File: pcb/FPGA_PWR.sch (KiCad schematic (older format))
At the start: 43 parts, among them U4 iCE40-HX8K-CT256, U8 AZ1117EH-ADJ

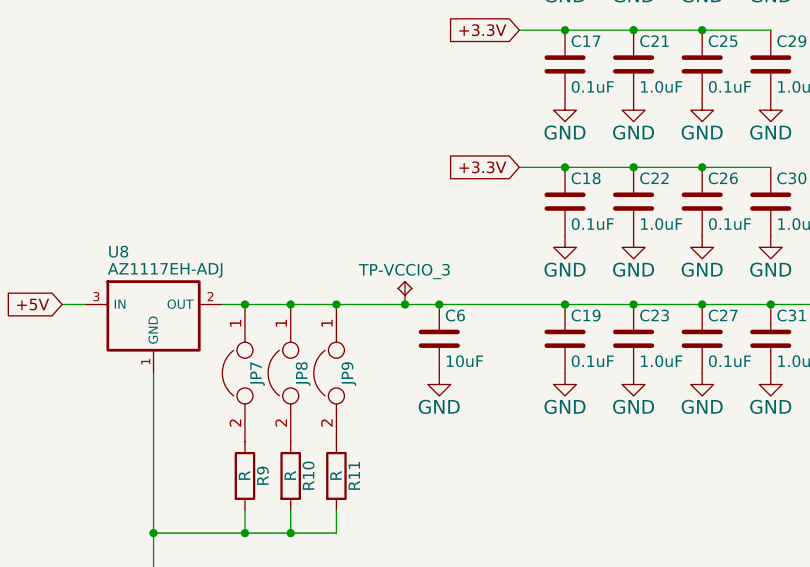
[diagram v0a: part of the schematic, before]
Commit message: Silkscreen done, test points added.
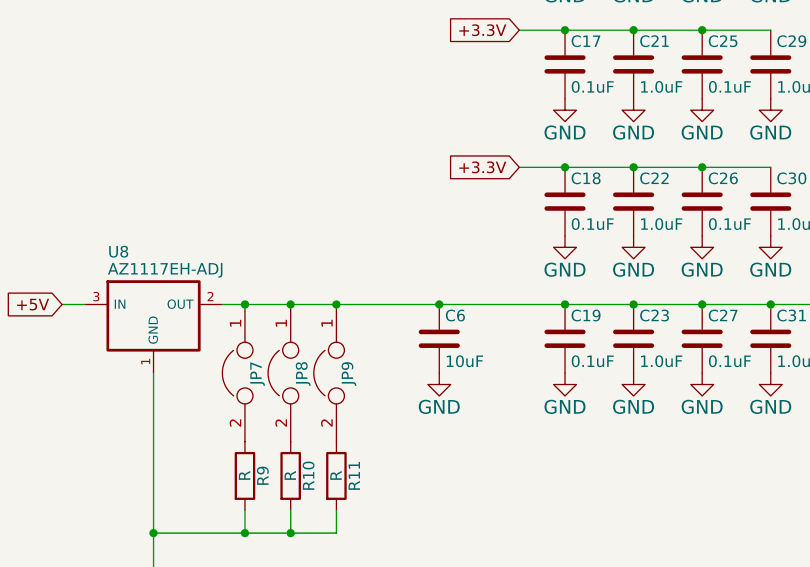
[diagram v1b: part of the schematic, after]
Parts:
- removed TP-VCCIO_3: TPTP-COMPACT, Measurement_Points:Measurement_Point_Round-TH_Small, symbol TPTP-COMPACT
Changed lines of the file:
@@
 1E 25 49 2A DA F6 C4 5C B7 0C C3 B9 A4 0A 98 09 FC 0D B0 92 CD 57 CD 1F 06 4E 04 26 A7 75 27 49
 52 39 26 13 73 DE C3 6C BE 70 B5 12 F8 16 86 73 8D C3 FF 03 63 F8 EE 2E BE 9A 04 B1 00 00 00 00
-49 45 4E 44 AE 42 60 82 73
+49 45 4E 44 AE 42 60 82 8C
 EndData
 $EndBitmap
@@
 $EndComp
 $Comp
-L TPTP-COMPACT TP-VCCIO_?
-U 1 1 55FBE808
-P 3500 5500
-AR Path="/55FBE808" Ref="TP-VCCIO_?"  Part="1"
-AR Path="/55DF5F27/55E883EA/55F049E0/55FBE808" Ref="TP-VCCIO_3"  Part="1"
-F 0 "TP-VCCIO_3" H 3500 5650 50  0000 C CNN
-F 1 "TPTP-COMPACT" H 3500 5500 50  0001 L BNN
-F 2 "Measurement_Points:Measurement_Point_Round-TH_Small" H 3500 5650 50  0001 C CNN
-F 3 "" H 3500 5500 60  0000 C CNN
-	1    3500 5500
-	1    0    0    -1
-$EndComp
-Connection ~ 3500 5500
-$Comp
 L C C6

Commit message: Generated the gerbers and submitted them. * Added some 3D models.
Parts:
- JP7, JP8, JP9: footprint open-project:S_JUMPER_2 -> XESS:S_JUMPER_2
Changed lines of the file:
@@
 1E 25 49 2A DA F6 C4 5C B7 0C C3 B9 A4 0A 98 09 FC 0D B0 92 CD 57 CD 1F 06 4E 04 26 A7 75 27 49
 52 39 26 13 73 DE C3 6C BE 70 B5 12 F8 16 86 73 8D C3 FF 03 63 F8 EE 2E BE 9A 04 B1 00 00 00 00
-49 45 4E 44 AE 42 60 82 8C
+49 45 4E 44 AE 42 60 82 40
 EndData
 $EndBitmap
@@
 F 0 "JP7" H 2800 5750 50  0000 C CNN
 F 1 "JUMPER" H 2800 5720 50  0001 C CNN
-F 2 "open-project:S_JUMPER_2" H 2800 5800 60  0001 C CNN
+F 2 "XESS:S_JUMPER_2" H 2800 5800 60  0001 C CNN
 F 3 "" H 2800 5800 60  0000 C CNN
 	1    2800 5800
@@
 F 0 "JP8" H 3000 5750 50  0000 C CNN
 F 1 "JUMPER" H 3000 5720 50  0001 C CNN
-F 2 "open-project:S_JUMPER_2" H 3000 5800 60  0001 C CNN
+F 2 "XESS:S_JUMPER_2" H 3000 5800 60  0001 C CNN
 F 3 "" H 3000 5800 60  0000 C CNN
 	1    3000 5800
@@
 F 0 "JP9" H 3200 5750 50  0000 C CNN
 F 1 "JUMPER" H 3200 5720 50  0001 C CNN
-F 2 "open-project:S_JUMPER_2" H 3200 5800 60  0001 C CNN
+F 2 "XESS:S_JUMPER_2" H 3200 5800 60  0001 C CNN
 F 3 "" H 3200 5800 60  0000 C CNN
 	1    3200 5800

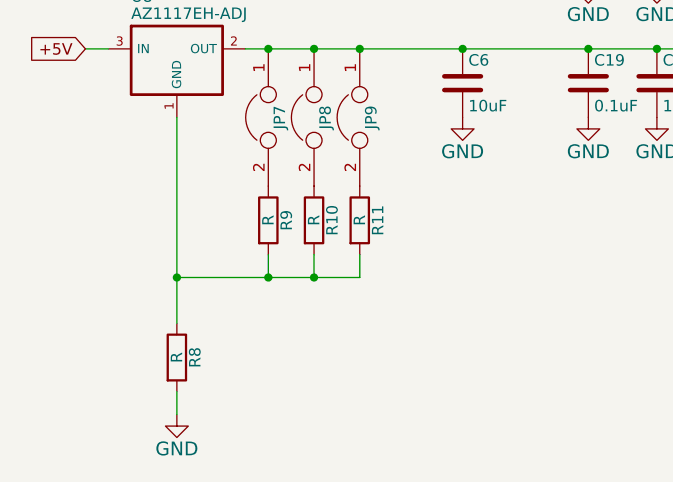
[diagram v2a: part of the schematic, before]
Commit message: Added manufacturer part numbers to the schematic.
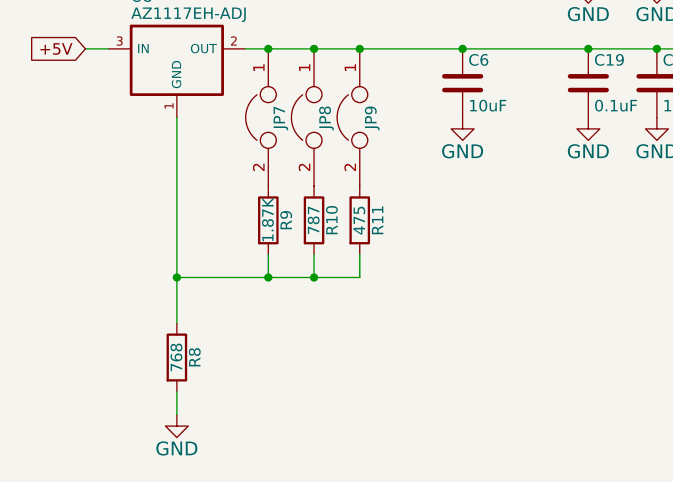
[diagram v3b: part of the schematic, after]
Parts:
- C16: manf# 08055C104KAT2A -> GRM188R71C104KA01D
- C17, C18, C19, C21, C22, C23, C24, C25, C26, C27, C28, C29, C30, C31, C32, C33, C34, C35, C38, C39, C40, C41, C42, C44, C45, C46: manf# 08055C104KAT2A -> (none)
- C20: manf# 08055C104KAT2A -> GRM188R71C105KE15D
- C43: manf# 08055C104KAT2A -> GRM188R71H103KA01D
- C6: manf# LMK212BJ106KD-T -> (none)
- D1: manf# (none) -> 1N4448WX-TP
- R10: value R -> 787; manf# (none) -> RC0603FR-07787RL
- R11: value R -> 475; manf# (none) -> RC0603FR-07475RL
- R8: value R -> 768; manf# (none) -> RC0603FR-07768RL
- R9: value R -> 1.87K; manf# (none) -> RC0603FR-071K87L
- U4: manf# (none) -> ICE40HX8K-CT256
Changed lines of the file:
@@
 F 2 "XESS:Lattice_caBGA_256" H 6700 2100 60  0001 C CNN
 F 3 "" H 6700 2100 60  0000 C CNN
+F 4 "ICE40HX8K-CT256" H 6700 2100 60  0001 C CNN "manf#"
 	1    6700 2100
 	1    0    0    -1
@@
 F 2 "Capacitors_SMD:C_0603" H 4238 3700 30  0001 C CNN
 F 3 "" H 4200 3850 60  0000 C CNN
-F 4 "08055C104KAT2A" H 4200 3850 60  0001 C CNN "manf#"
+F 4 "GRM188R71C104KA01D" H 4200 3850 60  0001 C CNN "manf#"
 	1    4200 3850
 	1    0    0    -1
@@
 F 2 "Capacitors_SMD:C_0603" H 4538 3700 30  0001 C CNN
 F 3 "" H 4500 3850 60  0000 C CNN
-F 4 "08055C104KAT2A" H 4500 3850 60  0001 C CNN "manf#"
+F 4 "GRM188R71C105KE15D" H 4500 3850 60  0001 C CNN "manf#"
 	1    4500 3850
 	1    0    0    -1
@@
 F 2 "Capacitors_SMD:C_0603" H 4838 3700 30  0001 C CNN
 F 3 "" H 4800 3850 60  0000 C CNN
-F 4 "08055C104KAT2A" H 4800 3850 60  0001 C CNN "manf#"
 	1    4800 3850
 	1    0    0    -1
@@
 F 2 "Capacitors_SMD:C_0603" H 5138 3700 30  0001 C CNN
 F 3 "" H 5100 3850 60  0000 C CNN
-F 4 "08055C104KAT2A" H 5100 3850 60  0001 C CNN "manf#"
 	1    5100 3850
 	1    0    0    -1
@@
 F 2 "Capacitors_SMD:C_0603" H 4238 4300 30  0001 C CNN
 F 3 "" H 4200 4450 60  0000 C CNN
-F 4 "08055C104KAT2A" H 4200 4450 60  0001 C CNN "manf#"
 	1    4200 4450
 	1    0    0    -1
@@
 F 2 "Capacitors_SMD:C_0603" H 4538 4300 30  0001 C CNN
 F 3 "" H 4500 4450 60  0000 C CNN
-F 4 "08055C104KAT2A" H 4500 4450 60  0001 C CNN "manf#"
 	1    4500 4450
 	1    0    0    -1
@@
 F 2 "Capacitors_SMD:C_0603" H 4838 4300 30  0001 C CNN
 F 3 "" H 4800 4450 60  0000 C CNN
-F 4 "08055C104KAT2A" H 4800 4450 60  0001 C CNN "manf#"
 	1    4800 4450
 	1    0    0    -1
@@
 F 2 "Capacitors_SMD:C_0603" H 5138 4300 30  0001 C CNN
 F 3 "" H 5100 4450 60  0000 C CNN
-F 4 "08055C104KAT2A" H 5100 4450 60  0001 C CNN "manf#"
 	1    5100 4450
 	1    0    0    -1
@@
 F 2 "Capacitors_SMD:C_0603" H 4238 4900 30  0001 C CNN
 F 3 "" H 4200 5050 60  0000 C CNN
-F 4 "08055C104KAT2A" H 4200 5050 60  0001 C CNN "manf#"
 	1    4200 5050
 	1    0    0    -1
@@
 F 2 "Capacitors_SMD:C_0603" H 4538 4900 30  0001 C CNN
 F 3 "" H 4500 5050 60  0000 C CNN
-F 4 "08055C104KAT2A" H 4500 5050 60  0001 C CNN "manf#"
 	1    4500 5050
 	1    0    0    -1
@@
 F 2 "Capacitors_SMD:C_0603" H 4838 4900 30  0001 C CNN
 F 3 "" H 4800 5050 60  0000 C CNN
-F 4 "08055C104KAT2A" H 4800 5050 60  0001 C CNN "manf#"
 	1    4800 5050
 	1    0    0    -1
@@
 F 2 "Capacitors_SMD:C_0603" H 5138 4900 30  0001 C CNN
 F 3 "" H 5100 5050 60  0000 C CNN
-F 4 "08055C104KAT2A" H 5100 5050 60  0001 C CNN "manf#"
 	1    5100 5050
 	1    0    0    -1
@@
 F 2 "Capacitors_SMD:C_0603" H 4238 5500 30  0001 C CNN
 F 3 "" H 4200 5650 60  0000 C CNN
-F 4 "08055C104KAT2A" H 4200 5650 60  0001 C CNN "manf#"
 	1    4200 5650
 	1    0    0    -1
@@
 F 2 "Capacitors_SMD:C_0603" H 4538 5500 30  0001 C CNN
 F 3 "" H 4500 5650 60  0000 C CNN
-F 4 "08055C104KAT2A" H 4500 5650 60  0001 C CNN "manf#"
 	1    4500 5650
 	1    0    0    -1
@@
 F 2 "Capacitors_SMD:C_0603" H 4838 5500 30  0001 C CNN
 F 3 "" H 4800 5650 60  0000 C CNN
-F 4 "08055C104KAT2A" H 4800 5650 60  0001 C CNN "manf#"
 	1    4800 5650
 	1    0    0    -1
@@
 F 2 "Capacitors_SMD:C_0603" H 5138 5500 30  0001 C CNN
 F 3 "" H 5100 5650 60  0000 C CNN
-F 4 "08055C104KAT2A" H 5100 5650 60  0001 C CNN "manf#"
 	1    5100 5650
 	1    0    0    -1
@@
 F 2 "Capacitors_SMD:C_0603" H 5588 1700 30  0001 C CNN
 F 3 "" H 5550 1850 60  0000 C CNN
-F 4 "08055C104KAT2A" H 5550 1850 60  0001 C CNN "manf#"
 	1    5550 1850
 	1    0    0    -1
@@
 F 2 "Capacitors_SMD:C_0805" H 5338 1700 30  0001 C CNN
 F 3 "" H 5300 1850 60  0000 C CNN
-F 4 "08055C104KAT2A" H 5300 1850 60  0001 C CNN "manf#"
 	1    5300 1850
 	1    0    0    -1
@@
 F 2 "Capacitors_SMD:C_0603" H 5588 2200 30  0001 C CNN
 F 3 "" H 5550 2350 60  0000 C CNN
-F 4 "08055C104KAT2A" H 5550 2350 60  0001 C CNN "manf#"
 	1    5550 2350
 	1    0    0    -1
@@
 F 2 "Capacitors_SMD:C_0805" H 5338 2200 30  0001 C CNN
 F 3 "" H 5300 2350 60  0000 C CNN
-F 4 "08055C104KAT2A" H 5300 2350 60  0001 C CNN "manf#"
 	1    5300 2350
 	1    0    0    -1
@@
 F 2 "Diodes_SMD:SOD-323" H 6550 2800 60  0001 C CNN
 F 3 "" H 6550 2800 60  0000 C CNN
+F 4 "1N4448WX-TP" H 6550 2800 60  0001 C CNN "manf#"
 	1    6550 2800
 	-1   0    0    1
@@
 F 2 "Capacitors_SMD:C_0603" H 6838 3700 30  0001 C CNN
 F 3 "" H 6800 3850 60  0000 C CNN
-F 4 "08055C104KAT2A" H 6800 3850 60  0001 C CNN "manf#"
 	1    6800 3850
 	1    0    0    -1
@@
 F 2 "Capacitors_SMD:C_0603" H 7138 3700 30  0001 C CNN
 F 3 "" H 7100 3850 60  0000 C CNN
-F 4 "08055C104KAT2A" H 7100 3850 60  0001 C CNN "manf#"
 	1    7100 3850
 	1    0    0    -1
@@
 F 2 "Capacitors_SMD:C_0603" H 7438 3700 30  0001 C CNN
 F 3 "" H 7400 3850 60  0000 C CNN
-F 4 "08055C104KAT2A" H 7400 3850 60  0001 C CNN "manf#"
 	1    7400 3850
 	1    0    0    -1
@@
 F 2 "Capacitors_SMD:C_0603" H 7738 3700 30  0001 C CNN
 F 3 "" H 7700 3850 60  0000 C CNN
-F 4 "08055C104KAT2A" H 7700 3850 60  0001 C CNN "manf#"
 	1    7700 3850
 	1    0    0    -1
@@
 F 2 "Capacitors_SMD:C_0603" H 8038 3700 30  0001 C CNN
 F 3 "" H 8000 3850 60  0000 C CNN
-F 4 "08055C104KAT2A" H 8000 3850 60  0001 C CNN "manf#"
 	1    8000 3850
 	1    0    0    -1
@@
 F 2 "Capacitors_SMD:C_0603" H 8338 3700 30  0001 C CNN
 F 3 "" H 8300 3850 60  0000 C CNN
-F 4 "08055C104KAT2A" H 8300 3850 60  0001 C CNN "manf#"
 	1    8300 3850
 	1    0    0    -1
@@
 F 2 "Capacitors_SMD:C_0603" H 6838 4300 30  0001 C CNN
 F 3 "" H 6800 4450 60  0000 C CNN
-F 4 "08055C104KAT2A" H 6800 4450 60  0001 C CNN "manf#"
 	1    6800 4450
 	1    0    0    -1
@@
 F 2 "Capacitors_SMD:C_0603" H 7138 4300 30  0001 C CNN
 F 3 "" H 7100 4450 60  0000 C CNN
-F 4 "08055C104KAT2A" H 7100 4450 60  0001 C CNN "manf#"
 	1    7100 4450
 	1    0    0    -1
@@
 F 2 "Capacitors_SMD:C_0603" H 7438 4300 30  0001 C CNN
 F 3 "" H 7400 4450 60  0000 C CNN
-F 4 "08055C104KAT2A" H 7400 4450 60  0001 C CNN "manf#"
+F 4 "GRM188R71H103KA01D" H 7400 4450 60  0001 C CNN "manf#"
 	1    7400 4450
 	1    0    0    -1
@@
 1E 25 49 2A DA F6 C4 5C B7 0C C3 B9 A4 0A 98 09 FC 0D B0 92 CD 57 CD 1F 06 4E 04 26 A7 75 27 49
 52 39 26 13 73 DE C3 6C BE 70 B5 12 F8 16 86 73 8D C3 FF 03 63 F8 EE 2E BE 9A 04 B1 00 00 00 00
-49 45 4E 44 AE 42 60 82 40
+49 45 4E 44 AE 42 60 82 13
 EndData
 $EndBitmap
@@
 F 2 "Capacitors_SMD:C_0805" H 3688 5500 30  0001 C CNN
 F 3 "" H 3650 5650 60  0000 C CNN
-F 4 "LMK212BJ106KD-T" H 3650 5650 60  0001 C CNN "manf#"
 	1    3650 5650
 	1    0    0    -1
@@
 P 2400 6850
 F 0 "R8" V 2480 6850 50  0000 C CNN
-F 1 "R" V 2400 6850 50  0000 C CNN
+F 1 "768" V 2400 6850 50  0000 C CNN
 F 2 "Resistors_SMD:R_0603" V 2330 6850 30  0001 C CNN
 F 3 "" H 2400 6850 30  0000 C CNN
+F 4 "RC0603FR-07768RL" V 2400 6850 60  0001 C CNN "manf#"
 	1    2400 6850
 	1    0    0    -1
@@
 P 2800 6250
 F 0 "R9" V 2880 6250 50  0000 C CNN
-F 1 "R" V 2800 6250 50  0000 C CNN
+F 1 "1.87K" V 2800 6250 50  0000 C CNN
 F 2 "Resistors_SMD:R_0603" V 2730 6250 30  0001 C CNN
 F 3 "" H 2800 6250 30  0000 C CNN
+F 4 "RC0603FR-071K87L" V 2800 6250 60  0001 C CNN "manf#"
 	1    2800 6250
 	1    0    0    -1
@@
 P 3000 6250
 F 0 "R10" V 3080 6250 50  0000 C CNN
-F 1 "R" V 3000 6250 50  0000 C CNN
+F 1 "787" V 3000 6250 50  0000 C CNN
 F 2 "Resistors_SMD:R_0603" V 2930 6250 30  0001 C CNN
 F 3 "" H 3000 6250 30  0000 C CNN
+F 4 "RC0603FR-07787RL" V 3000 6250 60  0001 C CNN "manf#"
 	1    3000 6250
 	1    0    0    -1
@@
 P 3200 6250
 F 0 "R11" V 3280 6250 50  0000 C CNN
-F 1 "R" V 3200 6250 50  0000 C CNN
+F 1 "475" V 3200 6250 50  0000 C CNN
 F 2 "Resistors_SMD:R_0603" V 3130 6250 30  0001 C CNN
 F 3 "" H 3200 6250 30  0000 C CNN
+F 4 "RC0603FR-07475RL" V 3200 6250 60  0001 C CNN "manf#"
 	1    3200 6250
 	1    0    0    -1

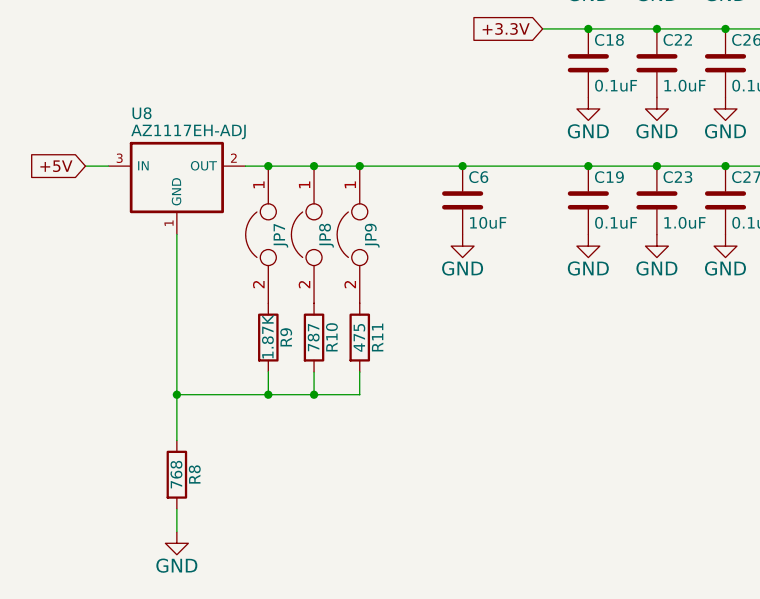
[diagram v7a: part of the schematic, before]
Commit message: Simplified resistor network for adjustable voltage regulator for VCCIO_3.
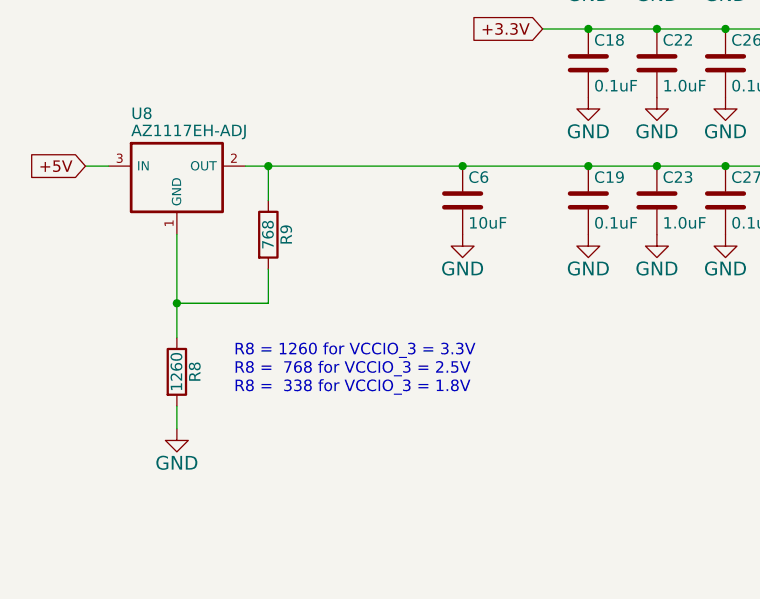
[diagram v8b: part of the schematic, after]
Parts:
- removed JP7, JP8, JP9: JUMPER, XESS:S_JUMPER_2, symbol JUMPER
- removed R10: 787, Resistors_SMD:R_0603, symbol R
- removed R11: 475, Resistors_SMD:R_0603, symbol R
- R8: value 768 -> 1260; footprint Resistors_SMD:R_0603 -> Resistors_SMD:R_0805_HandSoldering
- R9: value 1.87K -> 768
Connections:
- net VCCIO_3: now also R9.1
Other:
- note added: "R8 = 1260 for VCCIO_3 = 3.3V\nR8 = 768 for VCCIO_3 = 2.5V\nR8 = 338 for VCCIO_3 = 1.8V"
- moved on the sheet: R8, R9
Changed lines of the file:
@@
 1E 25 49 2A DA F6 C4 5C B7 0C C3 B9 A4 0A 98 09 FC 0D B0 92 CD 57 CD 1F 06 4E 04 26 A7 75 27 49
 52 39 26 13 73 DE C3 6C BE 70 B5 12 F8 16 86 73 8D C3 FF 03 63 F8 EE 2E BE 9A 04 B1 00 00 00 00
-49 45 4E 44 AE 42 60 82 4C
+49 45 4E 44 AE 42 60 82 5D
 EndData
 $EndBitmap
@@
 L GND #PWR049
 U 1 1 55FBE7FE
-P 2400 7100
-F 0 "#PWR049" H 2400 6850 60  0001 C CNN
-F 1 "GND" H 2400 6950 60  0000 C CNN
-F 2 "" H 2400 7100 60  0000 C CNN
-F 3 "" H 2400 7100 60  0000 C CNN
-	1    2400 7100
+P 2400 6650
+F 0 "#PWR049" H 2400 6400 60  0001 C CNN
+F 1 "GND" H 2400 6500 60  0000 C CNN
+F 2 "" H 2400 6650 60  0000 C CNN
+F 3 "" H 2400 6650 60  0000 C CNN
+	1    2400 6650
 	1    0    0    -1
 $EndComp
@@
 Connection ~ 3650 5500
 Wire Wire Line
-	2400 7100 2400 7000
+	2400 6650 2400 6550
 Wire Wire Line
-	2400 6700 2400 5800
+	2400 5800 2400 6250
 $Comp
 L R R8
 U 1 1 55FBE821
-P 2400 6850
-F 0 "R8" V 2480 6850 50  0000 C CNN
-F 1 "768" V 2400 6850 50  0000 C CNN
-F 2 "Resistors_SMD:R_0603" V 2330 6850 30  0001 C CNN
-F 3 "" H 2400 6850 30  0000 C CNN
-F 4 "RC0603FR-07768RL" V 2400 6850 60  0001 C CNN "manf#"
-	1    2400 6850
+P 2400 6400
+F 0 "R8" V 2480 6400 50  0000 C CNN
+F 1 "1260" V 2400 6400 50  0000 C CNN
+F 2 "Resistors_SMD:R_0805_HandSoldering" V 2330 6400 30  0001 C CNN
+F 3 "" H 2400 6400 30  0000 C CNN
+F 4 "RC0603FR-07768RL" V 2400 6400 60  0001 C CNN "manf#"
+	1    2400 6400
 	1    0    0    -1
 $EndComp
@@
 L R R9
 U 1 1 55FBE828
-P 2800 6250
-F 0 "R9" V 2880 6250 50  0000 C CNN
-F 1 "1.87K" V 2800 6250 50  0000 C CNN
-F 2 "Resistors_SMD:R_0603" V 2730 6250 30  0001 C CNN
-F 3 "" H 2800 6250 30  0000 C CNN
-F 4 "RC0603FR-071K87L" V 2800 6250 60  0001 C CNN "manf#"
-	1    2800 6250
+P 2800 5800
+F 0 "R9" V 2880 5800 50  0000 C CNN
+F 1 "768" V 2800 5800 50  0000 C CNN
+F 2 "Resistors_SMD:R_0603" V 2730 5800 30  0001 C CNN
+F 3 "" H 2800 5800 30  0000 C CNN
+F 4 "RC0603FR-071K87L" V 2800 5800 60  0001 C CNN "manf#"
+	1    2800 5800
 	1    0    0    -1
 $EndComp
-$Comp
-L R R10
-U 1 1 55FBE82F
-P 3000 6250
-F 0 "R10" V 3080 6250 50  0000 C CNN
-F 1 "787" V 3000 6250 50  0000 C CNN
-F 2 "Resistors_SMD:R_0603" V 2930 6250 30  0001 C CNN
-F 3 "" H 3000 6250 30  0000 C CNN
-F 4 "RC0603FR-07787RL" V 3000 6250 60  0001 C CNN "manf#"
-	1    3000 6250
-	1    0    0    -1
-$EndComp
-$Comp
-L R R11
-U 1 1 55FBE836
-P 3200 6250
-F 0 "R11" V 3280 6250 50  0000 C CNN
-F 1 "475" V 3200 6250 50  0000 C CNN
-F 2 "Resistors_SMD:R_0603" V 3130 6250 30  0001 C CNN
-F 3 "" H 3200 6250 30  0000 C CNN
-F 4 "RC0603FR-07475RL" V 3200 6250 60  0001 C CNN "manf#"
-	1    3200 6250
-	1    0    0    -1
-$EndComp
-$Comp
-L JUMPER JP7
-U 1 1 55FBE83D
-P 2800 5800
-F 0 "JP7" H 2800 5750 50  0000 C CNN
-F 1 "JUMPER" H 2800 5720 50  0001 C CNN
-F 2 "XESS:S_JUMPER_2" H 2800 5800 60  0001 C CNN
-F 3 "" H 2800 5800 60  0000 C CNN
-	1    2800 5800
-	0    -1   1    0
-$EndComp
-$Comp
-L JUMPER JP8
-U 1 1 55FBF618
-P 3000 5800
-F 0 "JP8" H 3000 5750 50  0000 C CNN
-F 1 "JUMPER" H 3000 5720 50  0001 C CNN
-F 2 "XESS:S_JUMPER_2" H 3000 5800 60  0001 C CNN
-F 3 "" H 3000 5800 60  0000 C CNN
-	1    3000 5800
-	0    -1   1    0
-$EndComp
-$Comp
-L JUMPER JP9
-U 1 1 55FBF6B6
-P 3200 5800
-F 0 "JP9" H 3200 5750 50  0000 C CNN
-F 1 "JUMPER" H 3200 5720 50  0001 C CNN
-F 2 "XESS:S_JUMPER_2" H 3200 5800 60  0001 C CNN
-F 3 "" H 3200 5800 60  0000 C CNN
-	1    3200 5800
-	0    -1   1    0
-$EndComp
-Connection ~ 2800 5500
-Connection ~ 3000 5500
-Connection ~ 3200 5500
-Wire Wire Line
-	2800 6400 2800 6500
-Wire Wire Line
-	2400 6500 3200 6500
-Connection ~ 2400 6500
-Wire Wire Line
-	3000 6500 3000 6400
-Connection ~ 2800 6500
-Wire Wire Line
-	3200 6500 3200 6400
-Connection ~ 3000 6500
 Wire Wire Line
 	2100 5500 2000 5500
 Text GLabel 2000 5500 0    50   Input ~ 0
 +5V
+Text Notes 2650 6500 0    50   ~ 0
+R8 = 1260 for VCCIO_3 = 3.3V\nR8 =  768 for VCCIO_3 = 2.5V\nR8 =  338 for VCCIO_3 = 1.8V
+Wire Wire Line
+	2800 5950 2800 6100
+Wire Wire Line
+	2800 6100 2400 6100
+Connection ~ 2400 6100
+Wire Wire Line
+	2800 5650 2800 5500
+Connection ~ 2800 5500
 $EndSCHEMATC
